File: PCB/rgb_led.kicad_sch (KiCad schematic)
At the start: 3 parts

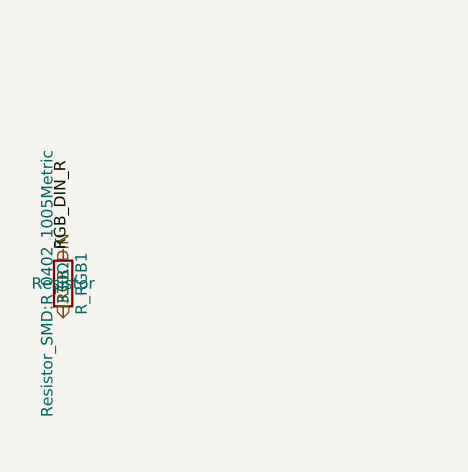
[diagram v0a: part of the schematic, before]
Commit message: task: swap R_RGB1 to Basic library (330R -> 470R)
The NeoPixel/SK6812 series resistor spec is a 300-500R range, not a
fixed value (see GPIO_table.md), so this doesn't need the divider-math
exercise the remaining Extended resistors (R_FB1/R_FB2/R_VSET1)
would -- 470R is a real Basic-library part (UNI-ROYAL 0402WGF4700TCE,
C25117) that fits comfortably in range, found via a wider/stricter
search than jlc_match.py's default after the 100R case showed its
default top-25 window can miss real matches.

Verified via kicad-cli sch export bom and sch erc (0 violations).

Co-Authored-By: Claude Sonnet 5 <noreply@anthropic.com>
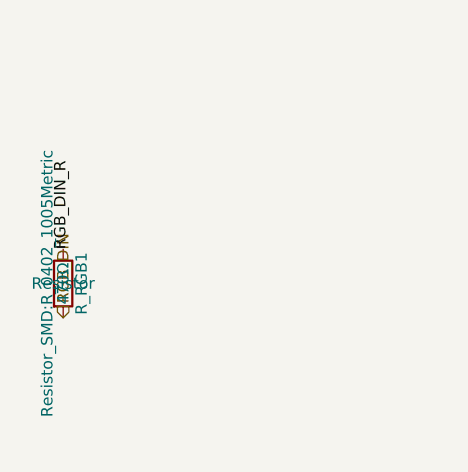
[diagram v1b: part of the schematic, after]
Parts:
- R_RGB1: value 330Ω -> 470Ω; LCSC C105875 -> C25117; MF Yageo -> UNI-ROYAL(Uniroyal Elec); Manufacturer_Part_Number RC0402FR-07330RL -> 0402WGF4700TCE
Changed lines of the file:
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@@
 			)
 		)
-		(property "Value" "330Ω"
+		(property "Value" "470Ω"
 			(at 121.92 130.81 90)
 			(show_name no)
@@
 			)
 		)
-		(property "MF" "Yageo"
+		(property "MF" "UNI-ROYAL(Uniroyal Elec)"
 			(at 0 0 0)
 			(hide yes)
@@
 			)
 		)
-		(property "Manufacturer_Part_Number" "RC0402FR-07330RL"
+		(property "Manufacturer_Part_Number" "0402WGF4700TCE"
 			(at 0 0 0)
 			(hide yes)
@@
 			)
 		)
-		(property "LCSC" "C105875"
+		(property "LCSC" "C25117"
 			(at 0 0 0)
 			(hide yes)

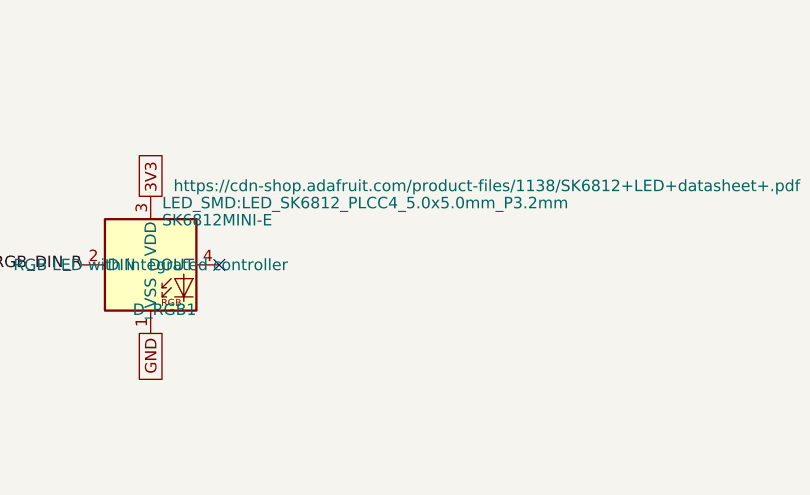
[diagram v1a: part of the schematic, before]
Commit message: fix: correct SK6812 RGB LED footprint mismatch that failed PCBWay assembly
D_RGB1 was still using a stale generic 5.0x5.0mm PLCC4 footprint left
over from before the design switched to the SK6812MINI-E, which is what
PCBWay's assembly check caught. Added a custom footprint sourced from
the real OPSCO SK6812MINI-E-012 datasheet, pointed the schematic at it,
and reworked the PCB placement/routing to match. DRC clean, 0 unconnected.

Co-Authored-By: Claude Sonnet 5 <noreply@anthropic.com>
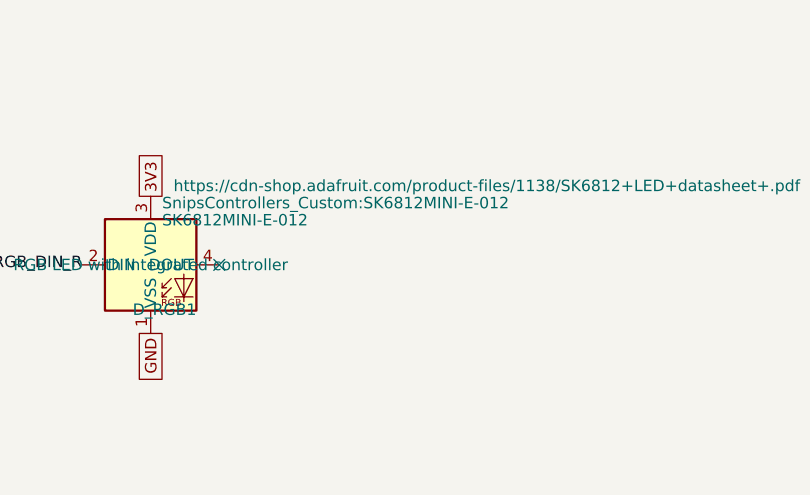
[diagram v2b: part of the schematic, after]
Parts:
- D_RGB1: value SK6812MINI-E -> SK6812MINI-E-012; footprint LED_SMD:LED_SK6812_PLCC4_5.0x5.0mm_P3.2mm -> SnipsControllers_Custom:SK6812MINI-E-012
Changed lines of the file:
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@@
 			)
 		)
-		(property "Value" "SK6812MINI-E"
+		(property "Value" "SK6812MINI-E-012"
 			(at 176.53 89.535 0)
 			(show_name no)
@@
 			)
 		)
-		(property "Footprint" "LED_SMD:LED_SK6812_PLCC4_5.0x5.0mm_P3.2mm"
+		(property "Footprint" "SnipsControllers_Custom:SK6812MINI-E-012"
 			(at 176.53 87.63 0)
 			(show_name no)

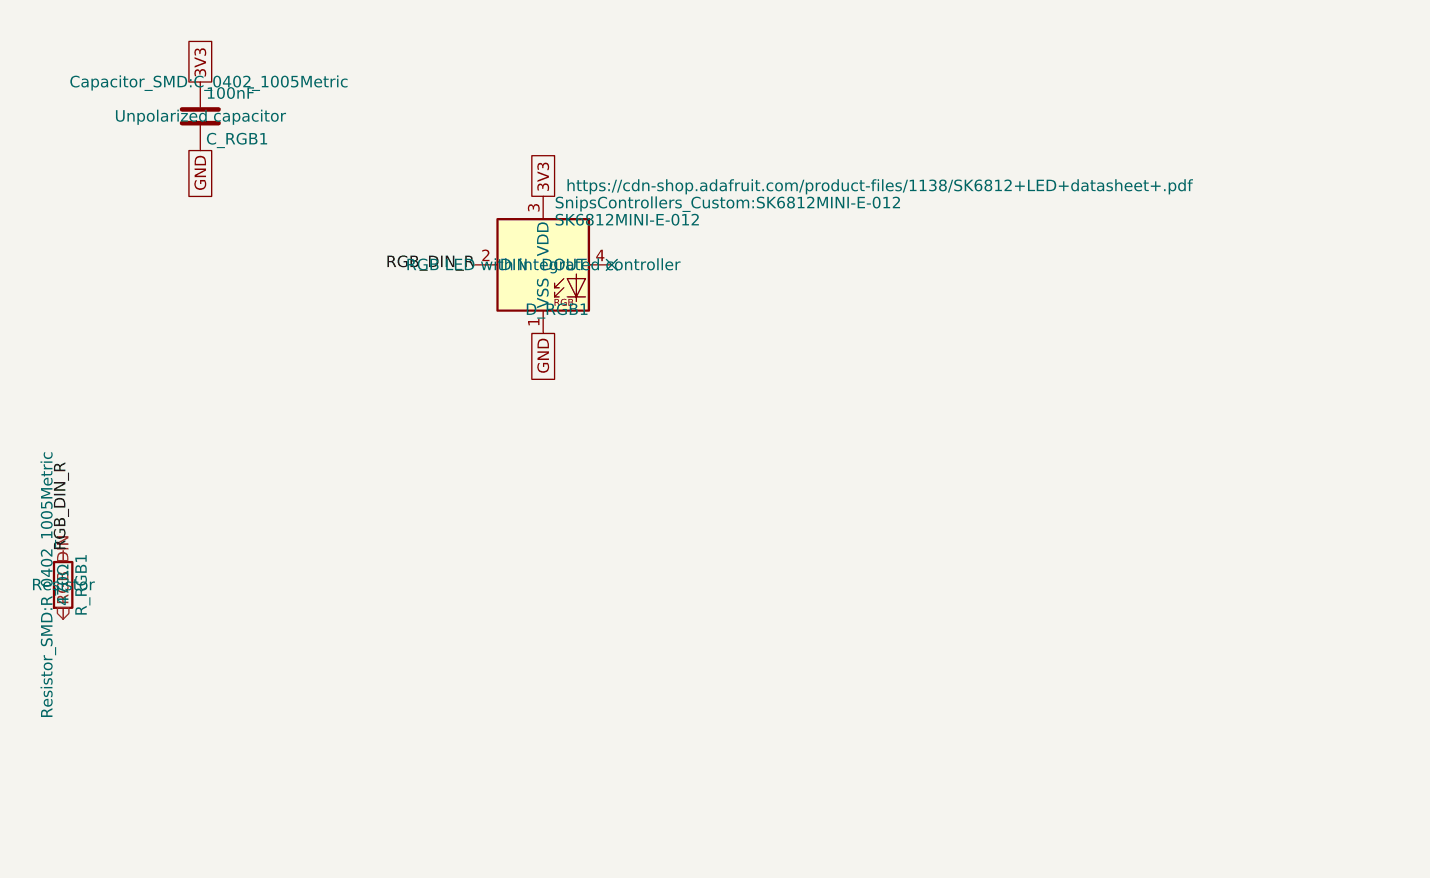
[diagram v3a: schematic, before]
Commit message: fix: make every BOM Value unambiguous for the fab, and switch D_INV_ISO1 to SOT-323 (#61)
* fix: make every BOM Value unambiguous for the fab, and switch D_INV_ISO1 to SOT-323

PCBWay flagged D_INV_ISO1: "BAT54W" is SOT-323 from nearly every maker, but we
had picked Yangjie's SOD-123 variant. A fab only sees Designator, Footprint,
Quantity and Value in the BOM (never MF/MPN/LCSC), so a bare part name is
ambiguous. Fixes the class of problem, not just this part:

- Every component's Value is now "<label> | <MPN> | <manufacturer> | <package>"
  (label dropped when it repeats the MPN; commas/periods stripped so the CSV
  never needs quoting). BT1 keeps its RIGHT-ANGLE HORIZONTAL note. Applied to
  all 81 parts across every sheet and the PCB.
- scripts/bom_values.py builds, applies, and checks these values, including
  that the PCB copy of Value/MF/MPN/footprint matches the schematic. New
  footprints must be added to its package table on purpose; hand-sourced parts
  with no MPN (J_STICK1) are listed explicitly.
- D_INV_ISO1 -> Diodes BAT54W-7-F in SOT-323 (common part, several makers).
  Pin 1 anode / pin 2 not connected / pin 3 cathode, confirmed against
  Nexperia's numbered pinning table and Diodes' datasheet. Uses KiCad's
  Diode:BAT54W symbol; PCB footprint replaced and rerouted. Electrically the
  same BAT54 family (30V, 200mA, 2uA leakage at 25V), so the SPICE model and
  scripts/spice/latch_sim.py still pass.
- Layout diagrams now say AO3401A for Q_PWR1 (they were stale since it was
  swapped from DMG2305UX) and BAT54W-7-F/SOT-323 for D_INV_ISO1.
- Repo CLAUDE.md documents the Value rule and the script.

ERC/DRC clean; production files regenerated.

Co-Authored-By: Claude Sonnet 5 <noreply@anthropic.com>

* chore: commit KiCad project settings (reordered used-designators list)

Co-Authored-By: Claude Sonnet 5 <noreply@anthropic.com>

---------

Co-authored-by: Claude Sonnet 5 <noreply@anthropic.com>
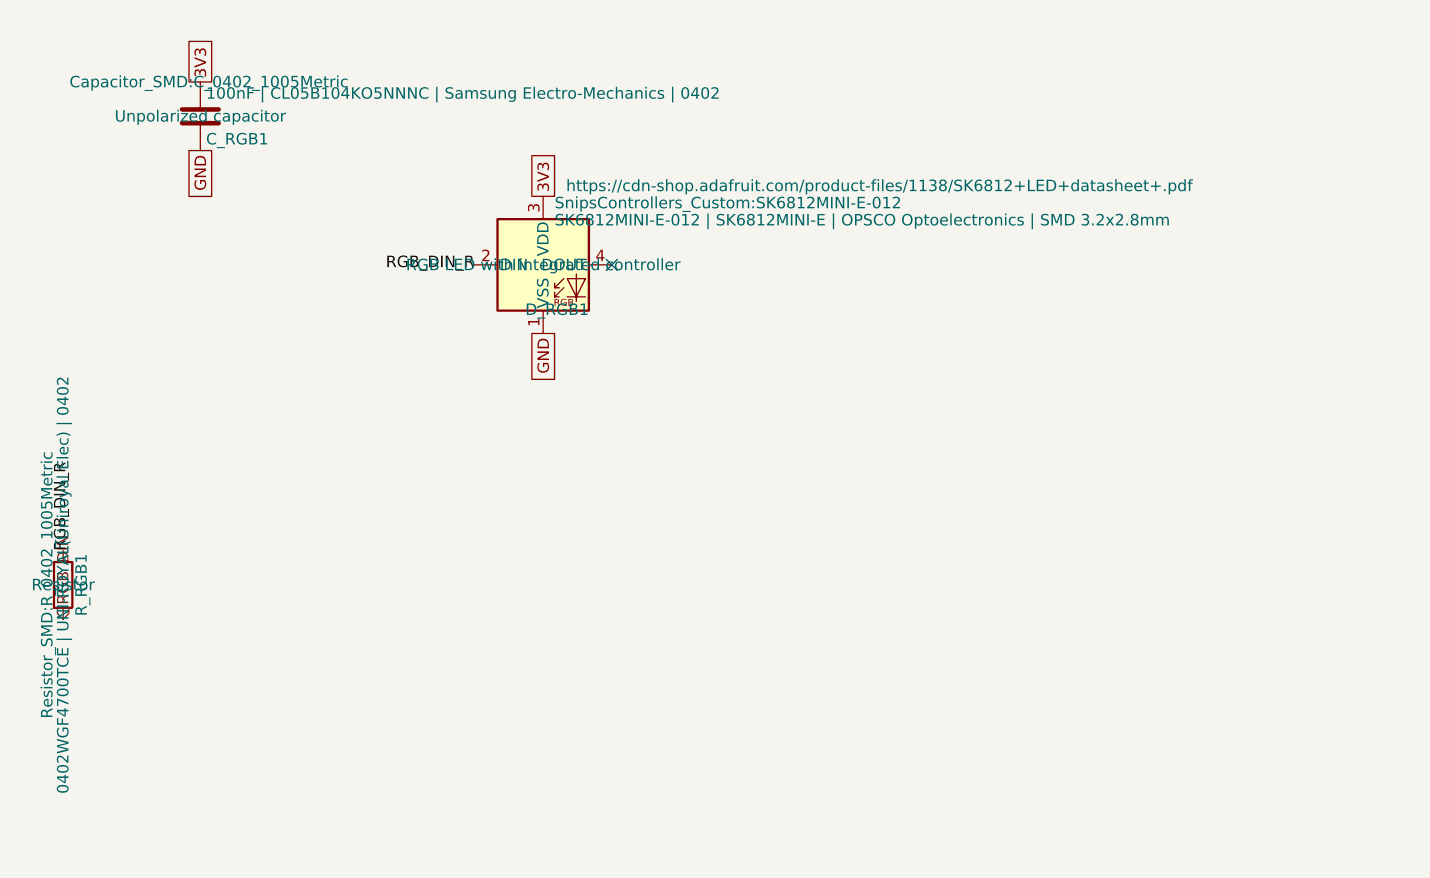
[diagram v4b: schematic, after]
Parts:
- C_RGB1: value 100nF -> 100nF | CL05B104KO5NNNC | Samsung Electro-Mechanics | 0402
- D_RGB1: value SK6812MINI-E-012 -> SK6812MINI-E-012 | SK6812MINI-E | OPSCO Optoelectronics | SMD 3.2x2.8mm
- R_RGB1: value 470Ω -> 0402WGF4700TCE | UNI-ROYAL(Uniroyal Elec) | 0402
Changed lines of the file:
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@@
 			)
 		)
-		(property "Value" "100nF"
+		(property "Value" "100nF | CL05B104KO5NNNC | Samsung Electro-Mechanics | 0402"
 			(at 137.795 76.2 0)
 			(show_name no)
@@
 			)
 		)
-		(property "Value" "470Ω"
+		(property "Value" "0402WGF4700TCE | UNI-ROYAL(Uniroyal Elec) | 0402"
 			(at 121.92 130.81 90)
 			(show_name no)
@@
 			)
 		)
-		(property "Value" "SK6812MINI-E-012"
+		(property "Value" "SK6812MINI-E-012 | SK6812MINI-E | OPSCO Optoelectronics | SMD 3.2x2.8mm"
 			(at 176.53 89.535 0)
 			(show_name no)
